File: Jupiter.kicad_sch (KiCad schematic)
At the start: 178 parts

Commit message: Finished LED matrix
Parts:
- added LED? (x82): SK6812MINI-E, marbastlib-various:LED_6028R, symbol marbastlib-various:SK6812MINI-E
- renumbered K-esc to K_esc
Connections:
- net +5V: now also LED?.1 (VDD), LED?.1 (VDD), LED?.1 (VDD), LED?.1 (VDD), LED?.1 (VDD), LED?.1 (VDD), LED?.1 (VDD), LED?.1 (VDD), LED?.1 (VDD), LED?.1 (VDD), LED?.1 (VDD), LED?.1 (VDD), LED?.1 (VDD), LED?.1 (VDD), LED?.1 (VDD), LED?.1 (VDD), LED?.1 (VDD), LED?.1 (VDD), LED?.1 (VDD), LED?.1 (VDD), LED?.1 (VDD), LED?.1 (VDD), LED?.1 (VDD), LED?.1 (VDD), LED?.1 (VDD), LED?.1 (VDD), LED?.1 (VDD), LED?.1 (VDD), LED?.1 (VDD), LED?.1 (VDD), LED?.1 (VDD), LED?.1 (VDD), LED?.1 (VDD), LED?.1 (VDD), LED?.1 (VDD), LED?.1 (VDD), LED?.1 (VDD), LED?.1 (VDD), LED?.1 (VDD), LED?.1 (VDD), LED?.1 (VDD), LED?.1 (VDD), LED?.1 (VDD), LED?.1 (VDD), LED?.1 (VDD), LED?.1 (VDD), LED?.1 (VDD), LED?.1 (VDD), LED?.1 (VDD), LED?.1 (VDD), LED?.1 (VDD), LED?.1 (VDD), LED?.1 (VDD), LED?.1 (VDD), LED?.1 (VDD), LED?.1 (VDD), LED?.1 (VDD), LED?.1 (VDD), LED?.1 (VDD), LED?.1 (VDD), LED?.1 (VDD), LED?.1 (VDD), LED?.1 (VDD), LED?.1 (VDD), LED?.1 (VDD), LED?.1 (VDD), LED?.1 (VDD), LED?.1 (VDD), LED?.1 (VDD), LED?.1 (VDD), LED?.1 (VDD), LED?.1 (VDD)
- net GND: now also LED?.4 (VSS), LED?.4 (VSS), LED?.4 (VSS), LED?.4 (VSS), LED?.4 (VSS), LED?.4 (VSS), LED?.4 (VSS), LED?.4 (VSS), LED?.4 (VSS), LED?.4 (VSS), LED?.4 (VSS), LED?.4 (VSS), LED?.4 (VSS), LED?.4 (VSS), LED?.4 (VSS), LED?.4 (VSS), LED?.4 (VSS), LED?.4 (VSS), LED?.4 (VSS), LED?.4 (VSS), LED?.4 (VSS), LED?.4 (VSS), LED?.4 (VSS), LED?.4 (VSS), LED?.4 (VSS), LED?.4 (VSS), LED?.4 (VSS), LED?.4 (VSS), LED?.4 (VSS), LED?.4 (VSS), LED?.4 (VSS), LED?.4 (VSS), LED?.4 (VSS), LED?.4 (VSS), LED?.4 (VSS), LED?.4 (VSS), LED?.4 (VSS), LED?.4 (VSS), LED?.4 (VSS), LED?.4 (VSS), LED?.4 (VSS), LED?.4 (VSS), LED?.4 (VSS), LED?.4 (VSS), LED?.4 (VSS), LED?.4 (VSS), LED?.4 (VSS), LED?.4 (VSS), LED?.4 (VSS), LED?.4 (VSS), LED?.4 (VSS), LED?.4 (VSS), LED?.4 (VSS), LED?.4 (VSS), LED?.4 (VSS), LED?.4 (VSS), LED?.4 (VSS), LED?.4 (VSS), LED?.4 (VSS), LED?.4 (VSS), LED?.4 (VSS), LED?.4 (VSS), LED?.4 (VSS), LED?.4 (VSS), LED?.4 (VSS), LED?.4 (VSS), LED?.4 (VSS), LED?.4 (VSS), LED?.4 (VSS), LED?.4 (VSS), LED?.4 (VSS), LED?.4 (VSS), LED?.4 (VSS), LED?.4 (VSS), LED?.4 (VSS), LED?.4 (VSS), LED?.4 (VSS), LED?.4 (VSS)
- new net: LED?.2 (DOUT), LED?.3 (DIN) (x81)
- new net: LED?.1 (VDD), LED?.1 (VDD), LED?.1 (VDD), LED?.1 (VDD), LED?.1 (VDD), LED?.1 (VDD), LED?.1 (VDD), LED?.1 (VDD), LED?.1 (VDD), LED?.1 (VDD)
- new net: LED?.4 (VSS), LED?.4 (VSS), LED?.4 (VSS), LED?.4 (VSS)
- new net RGBLED: LED?.3 (DIN)
- no-connect marks 1 -> 2
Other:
- moved on the sheet: C?, Q?, R?, SW?, U?, Y?

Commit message: labeled LED matrix
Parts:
- removed LED? (x2): SK6812MINI-E, marbastlib-various:LED_6028R, symbol marbastlib-various:SK6812MINI-E
- added LED_rightAlt, LED_rightControl: SK6812MINI-E, marbastlib-various:LED_6028R, symbol marbastlib-various:SK6812MINI-E
- gave numbers to parts that had none: 80
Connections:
- net +5V: now also LED_A.1 (VDD), LED_D.1 (VDD), LED_F.1 (VDD), LED_G.1 (VDD), LED_H.1 (VDD), LED_J.1 (VDD), LED_K.1 (VDD), LED_L.1 (VDD), LED_S.1 (VDD), LED_capsLock.1 (VDD), LED_rightAlt.1 (VDD), LED_rightControl.1 (VDD)
- net GND: now also LED_colon.4 (VSS), LED_enter.4 (VSS), LED_pgDn.4 (VSS), LED_quote.4 (VSS), LED_rightAlt.4 (VSS), LED_rightControl.4 (VSS)
- net at LED_space.3 (DIN): now also LED_rightAlt.2 (DOUT)
- net at LED_function.2 (DOUT): now also LED_rightAlt.3 (DIN)
- net at LED_leftArrow.2 (DOUT): now also LED_rightControl.3 (DIN); no longer LED_function.3 (DIN)
- net at LED_leftAlt.3 (DIN): now also LED_space.2 (DOUT)
- new net: LED_function.3 (DIN), LED_rightControl.2 (DOUT)

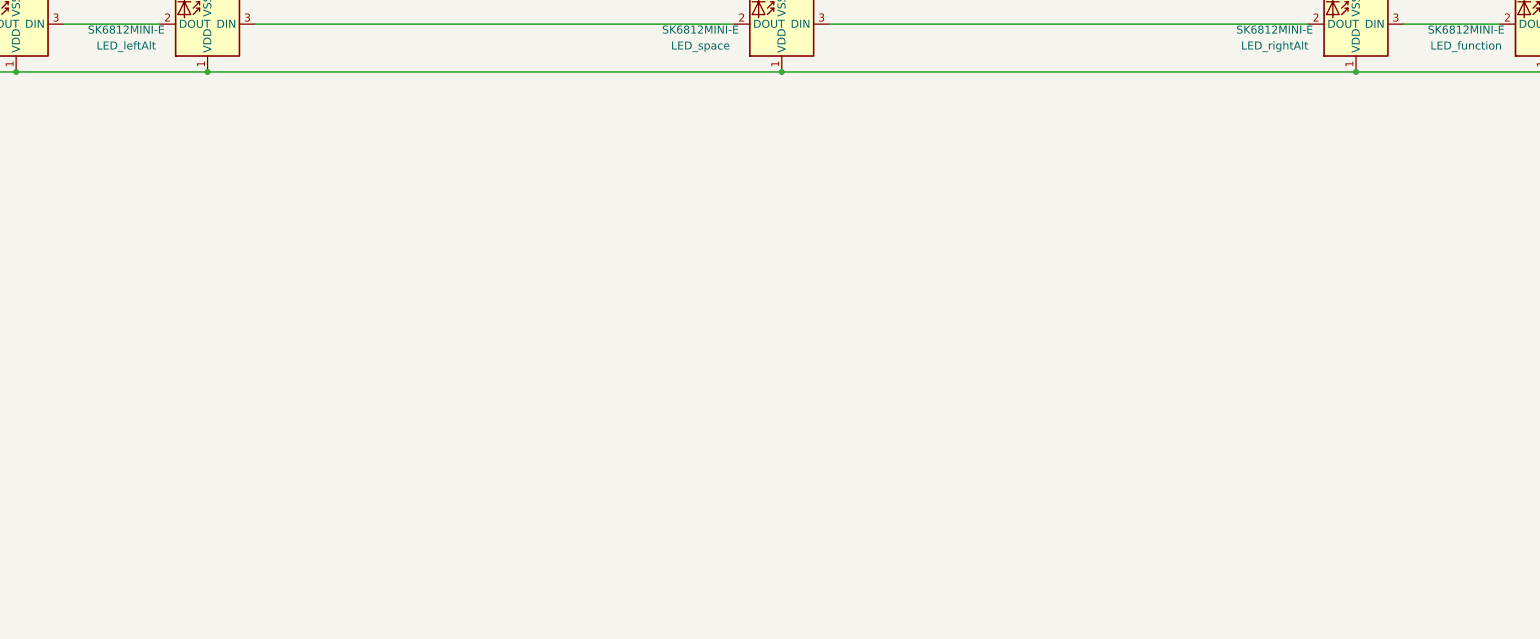
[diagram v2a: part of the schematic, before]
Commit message: Finished capacitor matrix
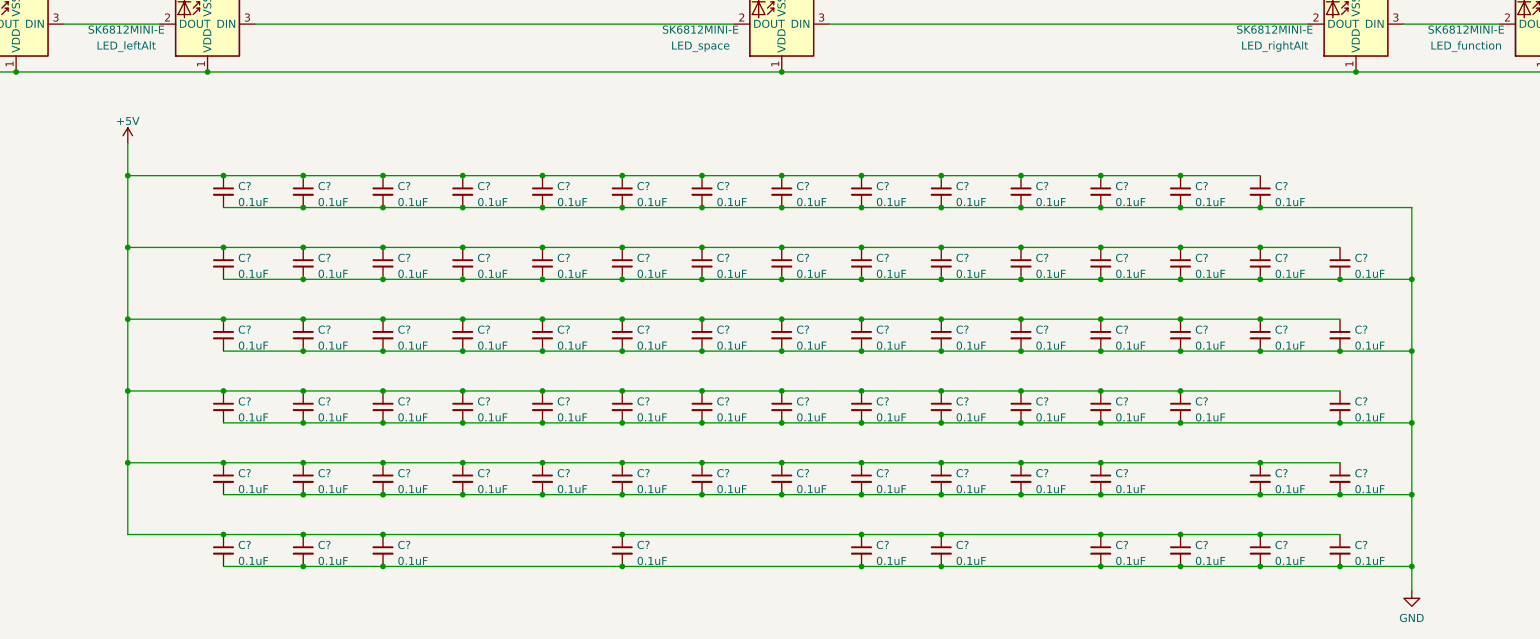
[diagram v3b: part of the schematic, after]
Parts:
- added C? (x82): 0.1uF, symbol Device:C_Small
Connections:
- net +5V: now also C?.1, C?.1, C?.1, C?.1, C?.1, C?.1, C?.1, C?.1, C?.1, C?.1, C?.1, C?.1, C?.1, C?.1, C?.1, C?.1, C?.1, C?.1, C?.1, C?.1, C?.1, C?.1, C?.1, C?.1, C?.1, C?.1, C?.1, C?.1, C?.1, C?.1, C?.1, C?.1, C?.1, C?.1, C?.1, C?.1, C?.1, C?.1, C?.1, C?.1, C?.1, C?.1, C?.1, C?.1, C?.1, C?.1, C?.1, C?.1, C?.1, C?.1, C?.1, C?.1, C?.1, C?.1, C?.1, C?.1, C?.1, C?.1, C?.1, C?.1, C?.1, C?.1, C?.1, C?.1, C?.1, C?.1, C?.1, C?.1, C?.1, C?.1, C?.1, C?.1, C?.1, C?.1, C?.1, C?.1, C?.1, C?.1, C?.1, C?.1, C?.1, C?.1
- net GND: now also C?.2, C?.2, C?.2, C?.2, C?.2, C?.2, C?.2, C?.2, C?.2, C?.2, C?.2, C?.2, C?.2, C?.2, C?.2, C?.2, C?.2, C?.2, C?.2, C?.2, C?.2, C?.2, C?.2, C?.2, C?.2, C?.2, C?.2, C?.2, C?.2, C?.2, C?.2, C?.2, C?.2, C?.2, C?.2, C?.2, C?.2, C?.2, C?.2, C?.2, C?.2, C?.2, C?.2, C?.2, C?.2, C?.2, C?.2, C?.2, C?.2, C?.2, C?.2, C?.2, C?.2, C?.2, C?.2, C?.2, C?.2, C?.2, C?.2, C?.2, C?.2, C?.2, C?.2, C?.2, C?.2, C?.2, C?.2, C?.2, C?.2, C?.2, C?.2, C?.2, C?.2, C?.2, C?.2, C?.2, C?.2, C?.2, C?.2, C?.2, C?.2, C?.2

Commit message: Added 4 pin connector for usb-c daughter board
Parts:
- removed Q?: 2N7002, Package_TO_SOT_SMD:SOT-23, symbol Transistor_FET:2N7002
- removed R?: 1k, symbol Device:R_Small
- added J?: Conn_01x04, symbol Connector_Generic:Conn_01x04
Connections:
- net +5V: now also J?.4 (Pin_4)
- net D+: now also J?.2 (Pin_2)
- net D-: now also J?.3 (Pin_3)
- net GND: now also J?.1 (Pin_1)
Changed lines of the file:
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@@
     (stroke (width 0) (type default) (color 0 0 0 0))
   )
+  (wire (pts (xy 504.19 72.39) (xy 504.19 74.93))
+    (stroke (width 0) (type default) (color 0 0 0 0))
+  )
   (wire (pts (xy 405.13 242.57) (xy 466.09 242.57))
     (stroke (width 0) (type default) (color 0 0 0 0))
@@
     (stroke (width 0) (type default) (color 0 0 0 0))
   )
+  (wire (pts (xy 511.81 64.77) (xy 504.19 64.77))
+    (stroke (width 0) (type default) (color 0 0 0 0))
+  )
   (wire (pts (xy 190.5 57.15) (xy 207.01 57.15))
     (stroke (width 0) (type default) (color 0 0 0 0))
@@
     (stroke (width 0) (type default) (color 0 0 0 0))
   )
+  (wire (pts (xy 494.03 62.23) (xy 504.19 62.23))
+    (stroke (width 0) (type default) (color 0 0 0 0))
+  )
   (wire (pts (xy 222.25 198.12) (xy 191.77 198.12))
     (stroke (width 0) (type default) (color 0 0 0 0))
@@
     (stroke (width 0) (type default) (color 0 0 0 0))
   )
+  (wire (pts (xy 511.81 72.39) (xy 504.19 72.39))
+    (stroke (width 0) (type default) (color 0 0 0 0))
+  )
   (wire (pts (xy 207.01 76.2) (xy 223.52 76.2))
     (stroke (width 0) (type default) (color 0 0 0 0))
@@
     (stroke (width 0) (type default) (color 0 0 0 0))
   )
+  (wire (pts (xy 504.19 64.77) (xy 504.19 62.23))
+    (stroke (width 0) (type default) (color 0 0 0 0))
+  )
   (wire (pts (xy 77.47 280.67) (xy 92.71 280.67))
     (stroke (width 0) (type default) (color 0 0 0 0))
@@
     (stroke (width 0) (type default) (color 0 0 0 0))
   )
+  (wire (pts (xy 494.03 74.93) (xy 504.19 74.93))
+    (stroke (width 0) (type default) (color 0 0 0 0))
+  )
   (wire (pts (xy 39.37 288.29) (xy 69.85 288.29))
     (stroke (width 0) (type default) (color 0 0 0 0))
@@
     (stroke (width 0) (type default) (color 0 0 0 0))
   )
-  (wire (pts (xy 391.16 52.07) (xy 407.67 52.07))
-    (stroke (width 0) (type default) (color 0 0 0 0))
-  )
   (wire (pts (xy 140.97 57.15) (xy 157.48 57.15))
     (stroke (width 0) (type default) (color 0 0 0 0))
@@
     )
   )
+  (global_label "D-" (shape input) (at 511.81 69.85 180) (fields_autoplaced)
+    (effects (font (size 1.27 1.27)) (justify right))
+    (property "Intersheet References" "${INTERSHEET_REFS}" (id 0) (at 506.5545 69.7706 0)
+      (effects (font (size 1.27 1.27)) (justify right) hide)
+    )
+  )
   (global_label "ROW4" (shape input) (at 29.21 114.3 180) (fields_autoplaced)
     (effects (font (size 1.27 1.27)) (justify right))
@@
     )
   )
-  (global_label "LEDGND" (shape input) (at 420.37 46.99 90) (fields_autoplaced)
-    (effects (font (size 1.27 1.27)) (justify left))
-    (property "Intersheet References" "${INTERSHEET_REFS}" (id 0) (at 420.2906 37.2593 90)
-      (effects (font (size 1.27 1.27)) (justify left) hide)
-    )
-  )
   (global_label "COL12" (shape input) (at 245.11 21.59 90) (fields_autoplaced)
     (effects (font (size 1.27 1.27)) (justify left))
@@
     )
   )
+  (global_label "D+" (shape input) (at 511.81 67.31 180) (fields_autoplaced)
+    (effects (font (size 1.27 1.27)) (justify right))
+    (property "Intersheet References" "${INTERSHEET_REFS}" (id 0) (at 506.5545 67.2306 0)
+      (effects (font (size 1.27 1.27)) (justify right) hide)
+    )
+  )
   (symbol (lib_id "Device:C_Small") (at 179.07 337.82 0) (unit 1)
     (in_bom yes) (on_board yes) (fields_autoplaced)
@@
     (pin "2")
   )
+  (symbol (lib_id "power:GND") (at 494.03 62.23 0) (unit 1)
+    (in_bom yes) (on_board yes) (fields_autoplaced)
+    (property "Reference" "#PWR?" (id 0) (at 494.03 68.58 0)
+      (effects (font (size 1.27 1.27)) hide)
+    )
+    (property "Value" "GND" (id 1) (at 494.03 66.6734 0))
+    (property "Footprint" "" (id 2) (at 494.03 62.23 0)
+      (effects (font (size 1.27 1.27)) hide)
+    )
+    (property "Datasheet" "" (id 3) (at 494.03 62.23 0)
+      (effects (font (size 1.27 1.27)) hide)
+    )
+    (pin "1")
+  )
   (symbol (lib_id "Device:C_Small") (at 166.37 360.68 0) (unit 1)
     (in_bom yes) (on_board yes) (fields_autoplaced)
@@
     (pin "2")
   )
-  (symbol (lib_id "power:GND") (at 420.37 57.15 0) (unit 1)
-    (in_bom yes) (on_board yes) (fields_autoplaced)
-    (property "Reference" "#PWR?" (id 0) (at 420.37 63.5 0)
-      (effects (font (size 1.27 1.27)) hide)
-    )
-    (property "Value" "GND" (id 1) (at 420.37 61.5934 0))
-    (property "Footprint" "" (id 2) (at 420.37 57.15 0)
-      (effects (font (size 1.27 1.27)) hide)
-    )
-    (property "Datasheet" "" (id 3) (at 420.37 57.15 0)
-      (effects (font (size 1.27 1.27)) hide)
-    )
-    (pin "1")
-  )
   (symbol (lib_id "Device:C_Small") (at 229.87 360.68 0) (unit 1)
     (in_bom yes) (on_board yes) (fields_autoplaced)
@@
     (pin "2")
   )
-  (symbol (lib_id "Device:R_Small") (at 410.21 52.07 90) (unit 1)
+  (symbol (lib_id "Connector_Generic:Conn_01x04") (at 516.89 67.31 0) (unit 1)
     (in_bom yes) (on_board yes) (fields_autoplaced)
-    (property "Reference" "R?" (id 0) (at 410.21 47.6336 90))
-    (property "Value" "1k" (id 1) (at 410.21 50.1705 90))
-    (property "Footprint" "" (id 2) (at 410.21 52.07 0)
+    (property "Reference" "J?" (id 0) (at 518.922 67.7453 0)
+      (effects (font (size 1.27 1.27)) (justify left))
+    )
+    (property "Value" "Conn_01x04" (id 1) (at 518.922 70.2822 0)
+      (effects (font (size 1.27 1.27)) (justify left))
+    )
+    (property "Footprint" "" (id 2) (at 516.89 67.31 0)
       (effects (font (size 1.27 1.27)) hide)
     )
-    (property "Datasheet" "~" (id 3) (at 410.21 52.07 0)
+    (property "Datasheet" "~" (id 3) (at 516.89 67.31 0)
       (effects (font (size 1.27 1.27)) hide)
     )
     (pin "1")
     (pin "2")
+    (pin "3")
+    (pin "4")
   )
   (symbol (lib_id "MX_Alps_Hybrid:MX-NoLED") (at 142.24 29.21 0) (unit 1)
@@
     (pin "2")
   )
+  (symbol (lib_id "power:+5V") (at 494.03 74.93 0) (unit 1)
+    (in_bom yes) (on_board yes) (fields_autoplaced)
+    (property "Reference" "#PWR?" (id 0) (at 494.03 78.74 0)
+      (effects (font (size 1.27 1.27)) hide)
+    )
+    (property "Value" "+5V" (id 1) (at 494.03 71.3542 0))
+    (property "Footprint" "" (id 2) (at 494.03 74.93 0)
+      (effects (font (size 1.27 1.27)) hide)
+    )
+    (property "Datasheet" "" (id 3) (at 494.03 74.93 0)
+      (effects (font (size 1.27 1.27)) hide)
+    )
+    (pin "1")
+  )
   (symbol (lib_id "MX_Alps_Hybrid:MX-NoLED") (at 208.28 67.31 0) (unit 1)
     (in_bom yes) (on_board yes) (fields_autoplaced)
@@
     (pin "2")
   )
-  (symbol (lib_id "Transistor_FET:2N7002") (at 417.83 52.07 0) (unit 1)
-    (in_bom yes) (on_board yes) (fields_autoplaced)
-    (property "Reference" "Q?" (id 0) (at 423.037 51.2353 0)
-      (effects (font (size 1.27 1.27)) (justify left))
-    )
-    (property "Value" "2N7002" (id 1) (at 423.037 53.7722 0)
-      (effects (font (size 1.27 1.27)) (justify left))
-    )
-    (property "Footprint" "Package_TO_SOT_SMD:SOT-23" (id 2) (at 422.91 53.975 0)
-      (effects (font (size 1.27 1.27) italic) (justify left) hide)
-    )
-    (property "Datasheet" "https://www.onsemi.com/pub/Collateral/NDS7002A-D.PDF" (id 3) (at 417.83 52.07 0)
-      (effects (font (size 1.27 1.27)) (justify left) hide)
-    )
-    (pin "1")
-    (pin "2")
-    (pin "3")
-  )
   (symbol (lib_id "marbastlib-various:SK6812MINI-E") (at 283.21 311.15 180) (unit 1)
     (in_bom yes) (on_board yes) (fields_autoplaced)
@@
       (reference "#PWR?") (unit 1) (value "GND") (footprint "")
     )
+    (path "/3a373b6e-dd93-4ce7-a5fa-c3f0eeb20393"
+      (reference "#PWR?") (unit 1) (value "GND") (footprint "")
+    )
     (path "/3e6f332d-1074-471a-a337-3b6f7ee82234"
       (reference "#PWR?") (unit 1) (value "GND") (footprint "")
@@
       (reference "#PWR?") (unit 1) (value "GND") (footprint "")
     )
-    (path "/619f2cb3-4f65-4c12-bba6-0a8289b83ea1"
-      (reference "#PWR?") (unit 1) (value "GND") (footprint "")
-    )
     (path "/765ae88e-2710-4dd3-8b7c-8459a6225d2e"
       (reference "#PWR?") (unit 1) (value "+5V") (footprint "")
@@
       (reference "#PWR?") (unit 1) (value "+5V") (footprint "")
     )
+    (path "/b1b843bb-0a51-472f-bfa0-76daff3f25f5"
+      (reference "#PWR?") (unit 1) (value "+5V") (footprint "")
+    )
     (path "/b685503f-af31-4124-b40f-55f706d85873"
       (reference "#PWR?") (unit 1) (value "+5V") (footprint "")
@@
       (reference "D?") (unit 1) (value "D_Small") (footprint "")
     )
+    (path "/94e4bd36-79cb-4b8d-812a-a19930d34fa5"
+      (reference "J?") (unit 1) (value "Conn_01x04") (footprint "")
+    )
     (path "/9de686b4-dca8-4f88-a6cb-b8703cee154a"
       (reference "K_0") (unit 1) (value "MX-NoLED") (footprint "")
@@
       (reference "LED_windows") (unit 1) (value "SK6812MINI-E") (footprint "marbastlib-various:LED_6028R")
     )
-    (path "/bf3216b5-086d-4c73-b437-59d860909c9b"
-      (reference "Q?") (unit 1) (value "2N7002") (footprint "Package_TO_SOT_SMD:SOT-23")
-    )
     (path "/3e21a20a-cf49-4f1b-85fb-a353e3bba35c"
       (reference "R?") (unit 1) (value "10k") (footprint "")
     )
-    (path "/95d9b2d2-e212-4f31-a20c-3852e32437d0"
-      (reference "R?") (unit 1) (value "1k") (footprint "")
-    )
     (path "/a18f4265-fb4f-470b-bcde-ceba57d3f6a4"

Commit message: Assigned Footprints
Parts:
- C1, C10, C11, C12, C13, C14, C15, C16, C17, C18, C19, C2, C20, C21, C22, C23, C24, C25, C26, C27, C28, C29, C3, C30, C31, C32, C33, C34, C35, C36, C37, C38, C39, C4, C40, C41, C42, C43, C44, C45, C46, C47, C48, C49, C5, C50, C51, C52, C53, C54, C55, C56, C57, C58, C59, C6, C60, C61, C62, C63, C64, C65, C66, C67, C68, C69, C7, C70, C71, C72, C73, C74, C75, C76, C77, C78, C79, C8, C80, C81, C82, C83, C84, C85, C86, C87, C88, C89, C9: renamed from C?; footprint (none) -> Capacitor_SMD:C_0603_1608Metric
- D1, D10, D11, D12, D13, D14, D15, D16, D17, D18, D19, D2, D20, D21, D22, D23, D24, D25, D26, D27, D28, D29, D3, D30, D31, D32, D33, D34, D35, D36, D37, D38, D39, D4, D40, D41, D42, D43, D44, D45, D46, D47, D48, D49, D5, D50, D51, D52, D53, D54, D55, D56, D57, D58, D59, D6, D60, D61, D62, D63, D64, D65, D66, D67, D68, D69, D7, D70, D71, D72, D73, D74, D75, D76, D77, D78, D79, D8, D80, D81, D82, D9: renamed from D?; footprint (none) -> Diode_SMD:D_0603_1608Metric
- J1: renamed from J?; footprint (none) -> random-keyboard-parts:JST-SR-4
- K_0, K_1, K_2, K_3, K_4, K_5, K_6, K_7, K_8, K_9, K_F1, K_F10, K_F11, K_F12, K_F2, K_F3, K_F4, K_F5, K_F6, K_F7, K_F8, K_F9: footprint (none) -> marbastlib-mx:SW_MX_HS_1u
- K_A1: renamed from K_A; footprint (none) -> marbastlib-mx:SW_MX_HS_1u
- K_B1: renamed from K_B; footprint (none) -> marbastlib-mx:SW_MX_HS_1u
- K_C1: renamed from K_C; footprint (none) -> marbastlib-mx:SW_MX_HS_1u
- K_D1: renamed from K_D; footprint (none) -> marbastlib-mx:SW_MX_HS_1u
- K_E1: renamed from K_E; footprint (none) -> marbastlib-mx:SW_MX_HS_1u
- K_F13: renamed from K_F; footprint (none) -> marbastlib-mx:SW_MX_HS_1u
- K_G1: renamed from K_G; footprint (none) -> marbastlib-mx:SW_MX_HS_1u
- K_H1: renamed from K_H; footprint (none) -> marbastlib-mx:SW_MX_HS_1u
- K_I1: renamed from K_I; footprint (none) -> marbastlib-mx:SW_MX_HS_1u
- K_J1: renamed from K_J; footprint (none) -> marbastlib-mx:SW_MX_HS_1u
- K_K1: renamed from K_K; footprint (none) -> marbastlib-mx:SW_MX_HS_1u
- K_L1: renamed from K_L; footprint (none) -> marbastlib-mx:SW_MX_HS_1u
- K_M1: renamed from K_M; footprint (none) -> marbastlib-mx:SW_MX_HS_1u
- K_N1: renamed from K_N; footprint (none) -> marbastlib-mx:SW_MX_HS_1u
- K_O1: renamed from K_O; footprint (none) -> marbastlib-mx:SW_MX_HS_1u
- K_P1: renamed from K_P; footprint (none) -> marbastlib-mx:SW_MX_HS_1u
- K_Q1: renamed from K_Q; footprint (none) -> marbastlib-mx:SW_MX_HS_1u
- K_R1: renamed from K_R; footprint (none) -> marbastlib-mx:SW_MX_HS_1u
- K_S1: renamed from K_S; footprint (none) -> marbastlib-mx:SW_MX_HS_1u
- K_T1: renamed from K_T; footprint (none) -> marbastlib-mx:SW_MX_HS_1u
- K_U1: renamed from K_U; footprint (none) -> marbastlib-mx:SW_MX_HS_1u
- K_V1: renamed from K_V; footprint (none) -> marbastlib-mx:SW_MX_HS_1u
- K_W1: renamed from K_W; footprint (none) -> marbastlib-mx:SW_MX_HS_1u
- K_X1: renamed from K_X; footprint (none) -> marbastlib-mx:SW_MX_HS_1u
- K_Y1: renamed from K_Y; footprint (none) -> marbastlib-mx:SW_MX_HS_1u
- K_Z1: renamed from K_Z; footprint (none) -> marbastlib-mx:SW_MX_HS_1u
- K_backSlash1: renamed from K_backSlash; footprint (none) -> marbastlib-mx:SW_MX_HS_1u
- K_backspace1: renamed from K_backspace; footprint (none) -> marbastlib-mx:SW_MX_HS_1u
- K_capsLock1: renamed from K_capsLock; footprint (none) -> marbastlib-mx:SW_MX_HS_1u
- K_closeBracket1: renamed from K_closeBracket; footprint (none) -> marbastlib-mx:SW_MX_HS_1u
- K_colon1: renamed from K_colon; footprint (none) -> marbastlib-mx:SW_MX_HS_1u
- K_comma1: renamed from K_comma; footprint (none) -> marbastlib-mx:SW_MX_HS_1u
- K_delete1: renamed from K_delete; footprint (none) -> marbastlib-mx:SW_MX_HS_1u
- K_downArrow1: renamed from K_downArrow; footprint (none) -> marbastlib-mx:SW_MX_HS_1u
- K_end1: renamed from K_end; footprint (none) -> marbastlib-mx:SW_MX_HS_1u
- K_enter1: renamed from K_enter; footprint (none) -> marbastlib-mx:SW_MX_HS_1u
- K_equals1: renamed from K_equals; footprint (none) -> marbastlib-mx:SW_MX_HS_1u
- K_esc1: renamed from K_esc; footprint (none) -> marbastlib-mx:SW_MX_HS_1u
- K_function1: renamed from K_function; footprint (none) -> marbastlib-mx:SW_MX_HS_1u
- K_home1: renamed from K_home; footprint (none) -> marbastlib-mx:SW_MX_HS_1u
- K_leftAlt1: renamed from K_leftAlt; footprint (none) -> marbastlib-mx:SW_MX_HS_1u
- K_leftArrow1: renamed from K_leftArrow; footprint (none) -> marbastlib-mx:SW_MX_HS_1u
- K_leftControl1: renamed from K_leftControl; footprint (none) -> marbastlib-mx:SW_MX_HS_1u
- K_leftShift1: renamed from K_leftShift; footprint (none) -> marbastlib-mx:SW_MX_HS_1u
- K_minus1: renamed from K_minus; footprint (none) -> marbastlib-mx:SW_MX_HS_1u
- K_openBracket1: renamed from K_openBracket; footprint (none) -> marbastlib-mx:SW_MX_HS_1u
- K_period1: renamed from K_period; footprint (none) -> marbastlib-mx:SW_MX_HS_1u
- K_pgDown1: renamed from K_pgDown; footprint (none) -> marbastlib-mx:SW_MX_HS_1u
- K_pgUp1: renamed from K_pgUp; footprint (none) -> marbastlib-mx:SW_MX_HS_1u
- K_questionMark1: renamed from K_questionMark; footprint (none) -> marbastlib-mx:SW_MX_HS_1u
- K_quote1: renamed from K_quote; footprint (none) -> marbastlib-mx:SW_MX_HS_1u
- K_rightAlt1: renamed from K_rightAlt; footprint (none) -> marbastlib-mx:SW_MX_HS_1u
- K_rightArrow1: renamed from K_rightArrow; footprint (none) -> marbastlib-mx:SW_MX_HS_1u
- K_rightControl1: renamed from K_rightControl; footprint (none) -> marbastlib-mx:SW_MX_HS_1u
- K_rightShift1: renamed from K_rightShift; footprint (none) -> marbastlib-mx:SW_MX_HS_1u
- K_space1: renamed from K_space; footprint (none) -> marbastlib-mx:SW_MX_HS_1u
- K_tab1: renamed from K_tab; footprint (none) -> marbastlib-mx:SW_MX_HS_1u
- K_tilda1: renamed from K_tilda; footprint (none) -> marbastlib-mx:SW_MX_HS_1u
- K_upArrow1: renamed from K_upArrow; footprint (none) -> marbastlib-mx:SW_MX_HS_1u
- K_windows1: renamed from K_windows; footprint (none) -> marbastlib-mx:SW_MX_HS_1u
- LED_0, LED_1, LED_2, LED_3, LED_4, LED_5, LED_6, LED_7, LED_8, LED_9, LED_F1, LED_F10, LED_F11, LED_F12, LED_F2, LED_F3, LED_F4, LED_F5, LED_F6, LED_F7, LED_F8, LED_F9: footprint marbastlib-various:LED_6028R -> marbastlib-mx:LED_MX_6028R
- LED_A1: renamed from LED_A; footprint marbastlib-various:LED_6028R -> marbastlib-mx:LED_MX_6028R
- LED_B1: renamed from LED_B; footprint marbastlib-various:LED_6028R -> marbastlib-mx:LED_MX_6028R
- LED_C1: renamed from LED_C; footprint marbastlib-various:LED_6028R -> marbastlib-mx:LED_MX_6028R
- LED_D1: renamed from LED_D; footprint marbastlib-various:LED_6028R -> marbastlib-mx:LED_MX_6028R
- LED_E1: renamed from LED_E; footprint marbastlib-various:LED_6028R -> marbastlib-mx:LED_MX_6028R
- LED_F13: renamed from LED_F; footprint marbastlib-various:LED_6028R -> marbastlib-mx:LED_MX_6028R
- LED_G1: renamed from LED_G; footprint marbastlib-various:LED_6028R -> marbastlib-mx:LED_MX_6028R
- LED_H1: renamed from LED_H; footprint marbastlib-various:LED_6028R -> marbastlib-mx:LED_MX_6028R
- LED_I1: renamed from LED_I; footprint marbastlib-various:LED_6028R -> marbastlib-mx:LED_MX_6028R
- LED_J1: renamed from LED_J; footprint marbastlib-various:LED_6028R -> marbastlib-mx:LED_MX_6028R
- LED_K1: renamed from LED_K; footprint marbastlib-various:LED_6028R -> marbastlib-mx:LED_MX_6028R
- LED_L1: renamed from LED_L; footprint marbastlib-various:LED_6028R -> marbastlib-mx:LED_MX_6028R
- LED_M1: renamed from LED_M; footprint marbastlib-various:LED_6028R -> marbastlib-mx:LED_MX_6028R
- LED_N1: renamed from LED_N; footprint marbastlib-various:LED_6028R -> marbastlib-mx:LED_MX_6028R
- LED_O1: renamed from LED_O; footprint marbastlib-various:LED_6028R -> marbastlib-mx:LED_MX_6028R
- LED_P1: renamed from LED_P; footprint marbastlib-various:LED_6028R -> marbastlib-mx:LED_MX_6028R
- LED_Q1: renamed from LED_Q; footprint marbastlib-various:LED_6028R -> marbastlib-mx:LED_MX_6028R
- LED_R1: renamed from LED_R; footprint marbastlib-various:LED_6028R -> marbastlib-mx:LED_MX_6028R
- LED_S1: renamed from LED_S; footprint marbastlib-various:LED_6028R -> marbastlib-mx:LED_MX_6028R
- LED_T1: renamed from LED_T; footprint marbastlib-various:LED_6028R -> marbastlib-mx:LED_MX_6028R
- LED_U1: renamed from LED_U; footprint marbastlib-various:LED_6028R -> marbastlib-mx:LED_MX_6028R
- LED_V1: renamed from LED_V; footprint marbastlib-various:LED_6028R -> marbastlib-mx:LED_MX_6028R
- LED_W1: renamed from LED_W; footprint marbastlib-various:LED_6028R -> marbastlib-mx:LED_MX_6028R
- LED_X1: renamed from LED_X; footprint marbastlib-various:LED_6028R -> marbastlib-mx:LED_MX_6028R
- LED_Y1: renamed from LED_Y; footprint marbastlib-various:LED_6028R -> marbastlib-mx:LED_MX_6028R
- LED_Z1: renamed from LED_Z; footprint marbastlib-various:LED_6028R -> marbastlib-mx:LED_MX_6028R
- LED_backslash1: renamed from LED_backslash; footprint marbastlib-various:LED_6028R -> marbastlib-mx:LED_MX_6028R
- LED_backspace1: renamed from LED_backspace; footprint marbastlib-various:LED_6028R -> marbastlib-mx:LED_MX_6028R
- LED_capsLock1: renamed from LED_capsLock; footprint marbastlib-various:LED_6028R -> marbastlib-mx:LED_MX_6028R
- LED_closeBracket1: renamed from LED_closeBracket; footprint marbastlib-various:LED_6028R -> marbastlib-mx:LED_MX_6028R
- LED_colon1: renamed from LED_colon; footprint marbastlib-various:LED_6028R -> marbastlib-mx:LED_MX_6028R
- LED_comma1: renamed from LED_comma; footprint marbastlib-various:LED_6028R -> marbastlib-mx:LED_MX_6028R
- LED_delete1: renamed from LED_delete; footprint marbastlib-various:LED_6028R -> marbastlib-mx:LED_MX_6028R
- LED_downArrow1: renamed from LED_downArrow; footprint marbastlib-various:LED_6028R -> marbastlib-mx:LED_MX_6028R
- LED_end1: renamed from LED_end; footprint marbastlib-various:LED_6028R -> marbastlib-mx:LED_MX_6028R
- LED_enter1: renamed from LED_enter; footprint marbastlib-various:LED_6028R -> marbastlib-mx:LED_MX_6028R
- LED_equals1: renamed from LED_equals; footprint marbastlib-various:LED_6028R -> marbastlib-mx:LED_MX_6028R
- LED_esc1: renamed from LED_esc; footprint marbastlib-various:LED_6028R -> marbastlib-mx:LED_MX_6028R
- LED_function1: renamed from LED_function; footprint marbastlib-various:LED_6028R -> marbastlib-mx:LED_MX_6028R
- LED_home1: renamed from LED_home; footprint marbastlib-various:LED_6028R -> marbastlib-mx:LED_MX_6028R
- LED_leftAlt1: renamed from LED_leftAlt; footprint marbastlib-various:LED_6028R -> marbastlib-mx:LED_MX_6028R
- LED_leftArrow1: renamed from LED_leftArrow; footprint marbastlib-various:LED_6028R -> marbastlib-mx:LED_MX_6028R
- LED_leftControl1: renamed from LED_leftControl; footprint marbastlib-various:LED_6028R -> marbastlib-mx:LED_MX_6028R
- LED_leftShift1: renamed from LED_leftShift; footprint marbastlib-various:LED_6028R -> marbastlib-mx:LED_MX_6028R
- LED_minus1: renamed from LED_minus; footprint marbastlib-various:LED_6028R -> marbastlib-mx:LED_MX_6028R
- LED_openBracket1: renamed from LED_openBracket; footprint marbastlib-various:LED_6028R -> marbastlib-mx:LED_MX_6028R
- LED_period1: renamed from LED_period; footprint marbastlib-various:LED_6028R -> marbastlib-mx:LED_MX_6028R
- LED_pgDn1: renamed from LED_pgDn; footprint marbastlib-various:LED_6028R -> marbastlib-mx:LED_MX_6028R
- LED_pgUp1: renamed from LED_pgUp; footprint marbastlib-various:LED_6028R -> marbastlib-mx:LED_MX_6028R
- LED_questionMark1: renamed from LED_questionMark; footprint marbastlib-various:LED_6028R -> marbastlib-mx:LED_MX_6028R
- LED_quote1: renamed from LED_quote; footprint marbastlib-various:LED_6028R -> marbastlib-mx:LED_MX_6028R
- LED_rightAlt1: renamed from LED_rightAlt; footprint marbastlib-various:LED_6028R -> marbastlib-mx:LED_MX_6028R
- LED_rightArrow1: renamed from LED_rightArrow; footprint marbastlib-various:LED_6028R -> marbastlib-mx:LED_MX_6028R
- LED_rightControl1: renamed from LED_rightControl; footprint marbastlib-various:LED_6028R -> marbastlib-mx:LED_MX_6028R
- LED_rightShift1: renamed from LED_rightShift; footprint marbastlib-various:LED_6028R -> marbastlib-mx:LED_MX_6028R
- LED_space1: renamed from LED_space; footprint marbastlib-various:LED_6028R -> marbastlib-mx:LED_MX_6028R
- LED_tab1: renamed from LED_tab; footprint marbastlib-various:LED_6028R -> marbastlib-mx:LED_MX_6028R
- LED_tilda1: renamed from LED_tilda; footprint marbastlib-various:LED_6028R -> marbastlib-mx:LED_MX_6028R
- LED_upArrow1: renamed from LED_upArrow; footprint marbastlib-various:LED_6028R -> marbastlib-mx:LED_MX_6028R
- LED_windows1: renamed from LED_windows; footprint marbastlib-various:LED_6028R -> marbastlib-mx:LED_MX_6028R
- R1, R2: renamed from R?; footprint (none) -> Resistor_SMD:R_0603_1608Metric
- SW1: renamed from SW?; footprint (none) -> random-keyboard-parts:SKQG-1155865
- Y1: renamed from Y?; footprint (none) -> Crystal:Crystal_SMD_3225-4Pin_3.2x2.5mm
- gave numbers to parts that had none: 1
